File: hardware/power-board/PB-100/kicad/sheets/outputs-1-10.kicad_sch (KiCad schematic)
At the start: 40 parts, among them J101 OUTPUT_CONNECTOR_CLASS_PRELIM, J102 OUTPUT_CONNECTOR_CLASS_PRELIM, J103 OUTPUT_CONNECTOR_CLASS_PRELIM, J104 OUTPUT_CONNECTOR_CLASS_PRELIM, J105 OUTPUT_CONNECTOR_CLASS_PRELIM, J106 OUTPUT_CONNECTOR_CLASS_PRELIM, J107 OUTPUT_CONNECTOR_CLASS_PRELIM, J108 OUTPUT_CONNECTOR_CLASS_PRELIM, J109 OUTPUT_CONNECTOR_CLASS_PRELIM, J110 OUTPUT_CONNECTOR_CLASS_PRELIM, Q101 SIDR626LDP_PRELIM, Q102 SIDR626LDP_PRELIM, Q103 SIDR626LDP_PRELIM, Q104 SIDR626LDP_PRELIM, Q105 SIDR626LDP_PRELIM, Q106 SIDR626LDP_PRELIM, Q107 SIDR626LDP_PRELIM, Q108 SIDR626LDP_PRELIM, Q109 SIDR626LDP_PRELIM, Q110 SIDR626LDP_PRELIM, U101 TPS48110AQDGXRQ1_PRELIM, U102 TPS48110AQDGXRQ1_PRELIM, U103 TPS48110AQDGXRQ1_PRELIM, U104 TPS48110AQDGXRQ1_PRELIM, U105 TPS48110AQDGXRQ1_PRELIM, U106 TPS48110AQDGXRQ1_PRELIM, U107 TPS48110AQDGXRQ1_PRELIM, U108 TPS48110AQDGXRQ1_PRELIM, U109 TPS48110AQDGXRQ1_PRELIM, U110 TPS48110AQDGXRQ1_PRELIM

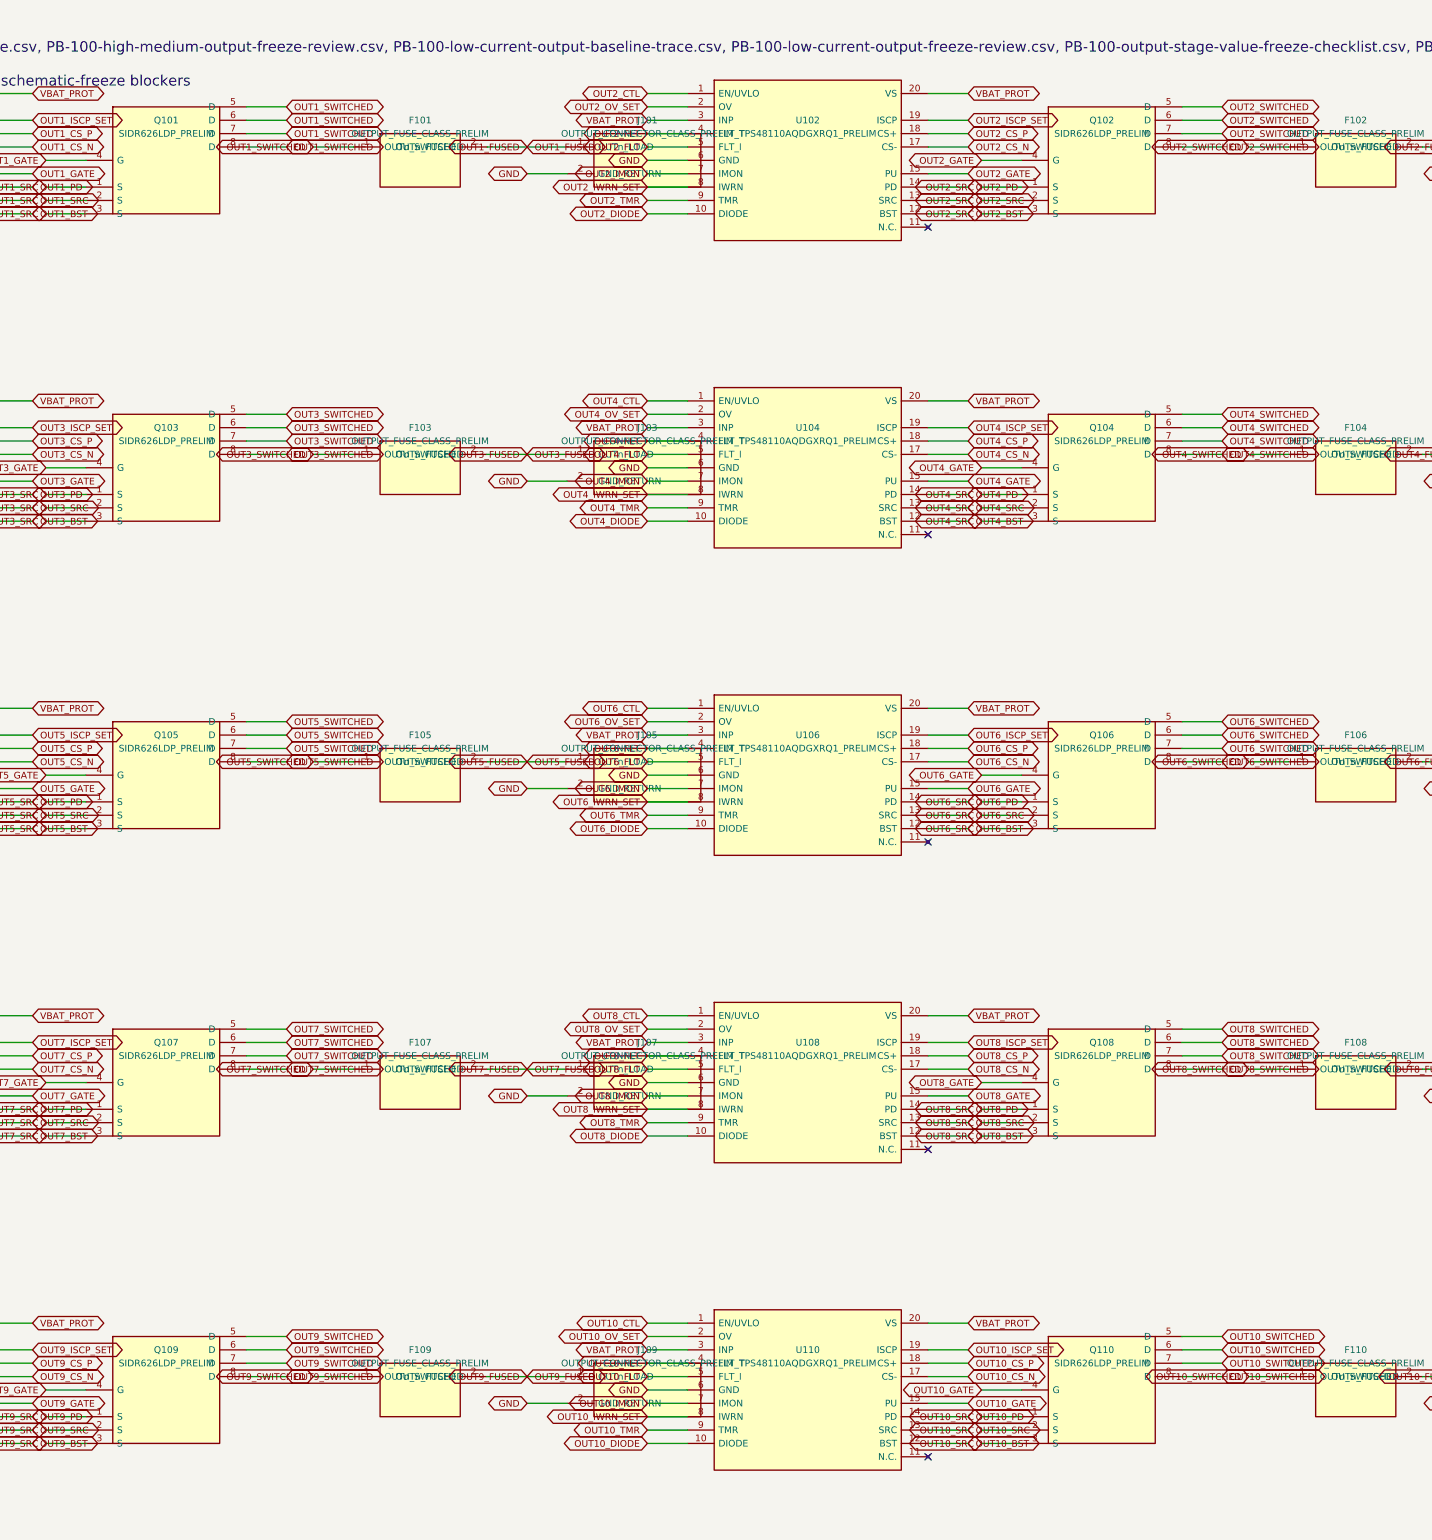
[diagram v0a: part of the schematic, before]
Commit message: feat(hardware): accept CAN1 and 80V freeze decisions
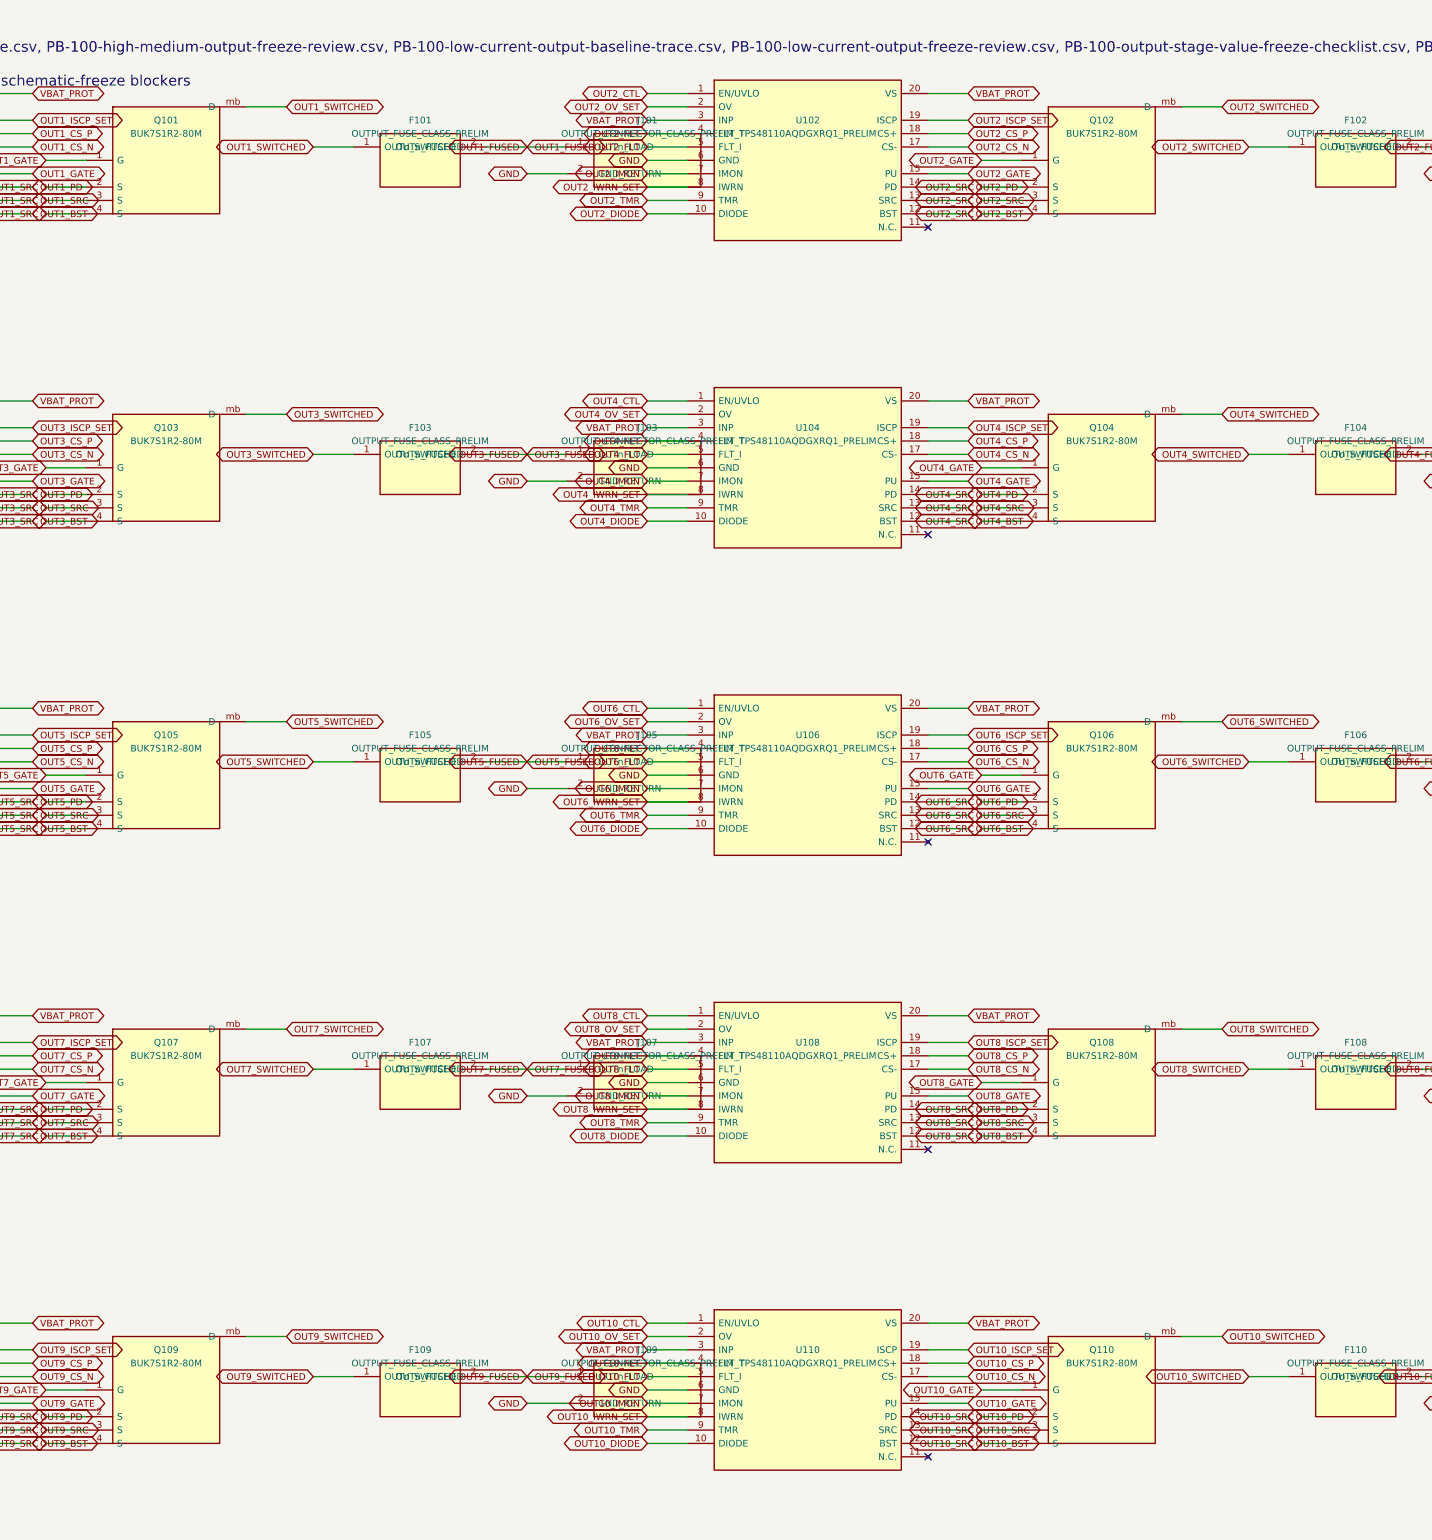
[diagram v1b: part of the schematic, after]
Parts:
- Q101, Q102, Q103, Q104, Q105, Q106, Q107, Q108, Q109, Q110: value SIDR626LDP_PRELIM -> BUK7S1R2-80M; footprint (none) -> PB100:LFPAK88_SOT1235_Nexperia; symbol PB100:PB100_SIDR626LDP_PRELIM -> PB100:PB100_POWER_NMOS_ESCAPE_PRELIM
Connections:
- net OUT10_GATE: now also Q110.1 (G); no longer Q110.4 (G)
- net OUT10_SRC: now also Q110.4 (S); no longer Q110.1 (S)
- net OUT10_SWITCHED: now also Q110.mb (D); no longer Q110.5 (D), Q110.6 (D), Q110.7 (D), Q110.8 (D)
- net OUT1_GATE: now also Q101.1 (G); no longer Q101.4 (G)
- net OUT1_SRC: now also Q101.4 (S); no longer Q101.1 (S)
- net OUT1_SWITCHED: now also Q101.mb (D); no longer Q101.5 (D), Q101.6 (D), Q101.7 (D), Q101.8 (D)
- net OUT2_GATE: now also Q102.1 (G); no longer Q102.4 (G)
- net OUT2_SRC: now also Q102.4 (S); no longer Q102.1 (S)
- net OUT2_SWITCHED: now also Q102.mb (D); no longer Q102.5 (D), Q102.6 (D), Q102.7 (D), Q102.8 (D)
- net OUT3_GATE: now also Q103.1 (G); no longer Q103.4 (G)
- net OUT3_SRC: now also Q103.4 (S); no longer Q103.1 (S)
- net OUT3_SWITCHED: now also Q103.mb (D); no longer Q103.5 (D), Q103.6 (D), Q103.7 (D), Q103.8 (D)
- net OUT4_GATE: now also Q104.1 (G); no longer Q104.4 (G)
- net OUT4_SRC: now also Q104.4 (S); no longer Q104.1 (S)
- net OUT4_SWITCHED: now also Q104.mb (D); no longer Q104.5 (D), Q104.6 (D), Q104.7 (D), Q104.8 (D)
- net OUT5_GATE: now also Q105.1 (G); no longer Q105.4 (G)
- net OUT5_SRC: now also Q105.4 (S); no longer Q105.1 (S)
- net OUT5_SWITCHED: now also Q105.mb (D); no longer Q105.5 (D), Q105.6 (D), Q105.7 (D), Q105.8 (D)
- net OUT6_GATE: now also Q106.1 (G); no longer Q106.4 (G)
- net OUT6_SRC: now also Q106.4 (S); no longer Q106.1 (S)
- net OUT6_SWITCHED: now also Q106.mb (D); no longer Q106.5 (D), Q106.6 (D), Q106.7 (D), Q106.8 (D)
- net OUT7_GATE: now also Q107.1 (G); no longer Q107.4 (G)
- net OUT7_SRC: now also Q107.4 (S); no longer Q107.1 (S)
- net OUT7_SWITCHED: now also Q107.mb (D); no longer Q107.5 (D), Q107.6 (D), Q107.7 (D), Q107.8 (D)
- net OUT8_GATE: now also Q108.1 (G); no longer Q108.4 (G)
- net OUT8_SRC: now also Q108.4 (S); no longer Q108.1 (S)
- net OUT8_SWITCHED: now also Q108.mb (D); no longer Q108.5 (D), Q108.6 (D), Q108.7 (D), Q108.8 (D)
- net OUT9_GATE: now also Q109.1 (G); no longer Q109.4 (G)
- net OUT9_SRC: now also Q109.4 (S); no longer Q109.1 (S)
- net OUT9_SWITCHED: now also Q109.mb (D); no longer Q109.5 (D), Q109.6 (D), Q109.7 (D), Q109.8 (D)

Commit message: feat(pb100): close five pre-layout blockers with generated evidence
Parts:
- Q101, Q102, Q103, Q104, Q105, Q106, Q107, Q108, Q109, Q110: value BUK7S1R2-80M -> IAUT300N08S5N012ATMA2; footprint PB100:LFPAK88_SOT1235_Nexperia -> PB100:PG-HSOF-8-1_TOLL_Infineon; symbol PB100:PB100_POWER_NMOS_ESCAPE_PRELIM -> PB100:PB100_POWER_NMOS_TOLL_80V
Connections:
- net OUT10_SRC: now also Q110.5 (S), Q110.6 (S), Q110.7 (S), Q110.8 (S)
- net OUT10_SWITCHED: now also Q110.Tab (D); no longer Q110.mb (D)
- net OUT1_SRC: now also Q101.5 (S), Q101.6 (S), Q101.7 (S), Q101.8 (S)
- net OUT1_SWITCHED: now also Q101.Tab (D); no longer Q101.mb (D)
- net OUT2_SRC: now also Q102.5 (S), Q102.6 (S), Q102.7 (S), Q102.8 (S)
- net OUT2_SWITCHED: now also Q102.Tab (D); no longer Q102.mb (D)
- net OUT3_SRC: now also Q103.5 (S), Q103.6 (S), Q103.7 (S), Q103.8 (S)
- net OUT3_SWITCHED: now also Q103.Tab (D); no longer Q103.mb (D)
- net OUT4_SRC: now also Q104.5 (S), Q104.6 (S), Q104.7 (S), Q104.8 (S)
- net OUT4_SWITCHED: now also Q104.Tab (D); no longer Q104.mb (D)
- net OUT5_SRC: now also Q105.5 (S), Q105.6 (S), Q105.7 (S), Q105.8 (S)
- net OUT5_SWITCHED: now also Q105.Tab (D); no longer Q105.mb (D)
- net OUT6_SRC: now also Q106.5 (S), Q106.6 (S), Q106.7 (S), Q106.8 (S)
- net OUT6_SWITCHED: now also Q106.Tab (D); no longer Q106.mb (D)
- net OUT7_SRC: now also Q107.5 (S), Q107.6 (S), Q107.7 (S), Q107.8 (S)
- net OUT7_SWITCHED: now also Q107.Tab (D); no longer Q107.mb (D)
- net OUT8_SRC: now also Q108.5 (S), Q108.6 (S), Q108.7 (S), Q108.8 (S)
- net OUT8_SWITCHED: now also Q108.Tab (D); no longer Q108.mb (D)
- net OUT9_SRC: now also Q109.5 (S), Q109.6 (S), Q109.7 (S), Q109.8 (S)
- net OUT9_SWITCHED: now also Q109.Tab (D); no longer Q109.mb (D)

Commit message: Advance PB-100 EVT routing baseline
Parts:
- removed F101, F102, F103, F104, F105, F106, F107, F108, F109, F110: OUTPUT_FUSE_CLASS_PRELIM, symbol PB100:PB100_OUTPUT_FUSE_CLASS_PRELIM
- removed J101, J102, J103, J104, J105, J106, J107, J108, J109, J110: OUTPUT_CONNECTOR_CLASS_PRELIM, symbol PB100:PB100_OUTPUT_CONNECTOR_CLASS_PRELIM
- removed Q101, Q102, Q103, Q104, Q105, Q106, Q107, Q108, Q109, Q110: IAUT300N08S5N012ATMA2, PB100:PG-HSOF-8-1_TOLL_Infineon, symbol PB100:PB100_POWER_NMOS_TOLL_80V
- removed U101, U102, U103, U104, U105, U106, U107, U108, U109, U110: TPS48110AQDGXRQ1_PRELIM, symbol PB100:PB100_TPS48110AQDGXRQ1_PRELIM
- added C1101: 680nF 16V X7R TMR, PB100:C0603, symbol PB100Gen:PB100G_C1101
- added C1102: 470nF 25V X7R BST, PB100:C0603, symbol PB100Gen:PB100G_C1102
- added C1103: 1nF 50V C0G ISCP, PB100:C0603, symbol PB100Gen:PB100G_C1103
- added C1104: 100nF 100V X7R VS, PB100:C0805, symbol PB100Gen:PB100G_C1104
- added C1105: 10nF 50V X7R IMON, PB100:C0603, symbol PB100Gen:PB100G_C1105
- added C1106: 1nF 25V DNP GATE-SLEW, PB100:C0603, symbol PB100Gen:PB100G_C1106
- added C1107: 1nF 100V C0G DNP SNUBBER, PB100:C0603, symbol PB100Gen:PB100G_C1107
- added C1201: 680nF 16V X7R TMR, PB100:C0603, symbol PB100Gen:PB100G_C1201
- added C1202: 470nF 25V X7R BST, PB100:C0603, symbol PB100Gen:PB100G_C1202
- added C1203: 1nF 50V C0G ISCP, PB100:C0603, symbol PB100Gen:PB100G_C1203
- added C1204: 100nF 100V X7R VS, PB100:C0805, symbol PB100Gen:PB100G_C1204
- added C1205: 10nF 50V X7R IMON, PB100:C0603, symbol PB100Gen:PB100G_C1205
- added C1206: 1nF 25V DNP GATE-SLEW, PB100:C0603, symbol PB100Gen:PB100G_C1206
- added C1207: 1nF 100V C0G DNP SNUBBER, PB100:C0603, symbol PB100Gen:PB100G_C1207
- added C1301: 680nF 16V X7R TMR, PB100:C0603, symbol PB100Gen:PB100G_C1301
- added C1302: 470nF 25V X7R BST, PB100:C0603, symbol PB100Gen:PB100G_C1302
- added C1303: 1nF 50V C0G ISCP, PB100:C0603, symbol PB100Gen:PB100G_C1303
- added C1304: 100nF 100V X7R VS, PB100:C0805, symbol PB100Gen:PB100G_C1304
- added C1305: 10nF 50V X7R IMON, PB100:C0603, symbol PB100Gen:PB100G_C1305
- added C1306: 1nF 25V DNP GATE-SLEW, PB100:C0603, symbol PB100Gen:PB100G_C1306
- added C1307: 1nF 100V C0G DNP SNUBBER, PB100:C0603, symbol PB100Gen:PB100G_C1307
- added C1401: 680nF 16V X7R TMR, PB100:C0603, symbol PB100Gen:PB100G_C1401
- added C1402: 470nF 25V X7R BST, PB100:C0603, symbol PB100Gen:PB100G_C1402
- added C1403: 1nF 50V C0G ISCP, PB100:C0603, symbol PB100Gen:PB100G_C1403
- added C1404: 100nF 100V X7R VS, PB100:C0805, symbol PB100Gen:PB100G_C1404
- added C1405: 10nF 50V X7R IMON, PB100:C0603, symbol PB100Gen:PB100G_C1405
- added C1406: 1nF 25V DNP GATE-SLEW, PB100:C0603, symbol PB100Gen:PB100G_C1406
- added C1407: 1nF 100V C0G DNP SNUBBER, PB100:C0603, symbol PB100Gen:PB100G_C1407
- added C1501: 680nF 16V X7R TMR, PB100:C0603, symbol PB100Gen:PB100G_C1501
- added C1502: 470nF 25V X7R BST, PB100:C0603, symbol PB100Gen:PB100G_C1502
- added C1503: 1nF 50V C0G ISCP, PB100:C0603, symbol PB100Gen:PB100G_C1503
- added C1504: 100nF 100V X7R VS, PB100:C0805, symbol PB100Gen:PB100G_C1504
- added C1505: 10nF 50V X7R IMON, PB100:C0603, symbol PB100Gen:PB100G_C1505
- added C1506: 1nF 25V DNP GATE-SLEW, PB100:C0603, symbol PB100Gen:PB100G_C1506
- added C1507: 1nF 100V C0G DNP SNUBBER, PB100:C0603, symbol PB100Gen:PB100G_C1507
- added C1601: 680nF 16V X7R TMR, PB100:C0603, symbol PB100Gen:PB100G_C1601
- added C1602: 470nF 25V X7R BST, PB100:C0603, symbol PB100Gen:PB100G_C1602
- added C1603: 1nF 50V C0G ISCP, PB100:C0603, symbol PB100Gen:PB100G_C1603
- added C1604: 100nF 100V X7R VS, PB100:C0805, symbol PB100Gen:PB100G_C1604
- added C1605: 10nF 50V X7R IMON, PB100:C0603, symbol PB100Gen:PB100G_C1605
- added C1606: 1nF 25V DNP GATE-SLEW, PB100:C0603, symbol PB100Gen:PB100G_C1606
- added C1607: 1nF 100V C0G DNP SNUBBER, PB100:C0603, symbol PB100Gen:PB100G_C1607
- added C1701: 680nF 16V X7R TMR, PB100:C0603, symbol PB100Gen:PB100G_C1701
- added C1702: 470nF 25V X7R BST, PB100:C0603, symbol PB100Gen:PB100G_C1702
- added C1703: 1nF 50V C0G ISCP, PB100:C0603, symbol PB100Gen:PB100G_C1703
- added C1704: 100nF 100V X7R VS, PB100:C0805, symbol PB100Gen:PB100G_C1704
- added C1705: 10nF 50V X7R IMON, PB100:C0603, symbol PB100Gen:PB100G_C1705
- added C1706: 1nF 25V DNP GATE-SLEW, PB100:C0603, symbol PB100Gen:PB100G_C1706
- added C1707: 1nF 100V C0G DNP SNUBBER, PB100:C0603, symbol PB100Gen:PB100G_C1707
- added C1801: 680nF 16V X7R TMR, PB100:C0603, symbol PB100Gen:PB100G_C1801
- added C1802: 470nF 25V X7R BST, PB100:C0603, symbol PB100Gen:PB100G_C1802
- added C1803: 1nF 50V C0G ISCP, PB100:C0603, symbol PB100Gen:PB100G_C1803
- added C1804: 100nF 100V X7R VS, PB100:C0805, symbol PB100Gen:PB100G_C1804
- added C1805: 10nF 50V X7R IMON, PB100:C0603, symbol PB100Gen:PB100G_C1805
- added C1806: 1nF 25V DNP GATE-SLEW, PB100:C0603, symbol PB100Gen:PB100G_C1806
- added C1807: 1nF 100V C0G DNP SNUBBER, PB100:C0603, symbol PB100Gen:PB100G_C1807
- added C1901: 680nF 16V X7R TMR, PB100:C0603, symbol PB100Gen:PB100G_C1901
- added C1902: 470nF 25V X7R BST, PB100:C0603, symbol PB100Gen:PB100G_C1902
- added C1903: 1nF 50V C0G ISCP, PB100:C0603, symbol PB100Gen:PB100G_C1903
- added C1904: 100nF 100V X7R VS, PB100:C0805, symbol PB100Gen:PB100G_C1904
- added C1905: 10nF 50V X7R IMON, PB100:C0603, symbol PB100Gen:PB100G_C1905
- added C1906: 1nF 25V DNP GATE-SLEW, PB100:C0603, symbol PB100Gen:PB100G_C1906
- added C1907: 1nF 100V C0G DNP SNUBBER, PB100:C0603, symbol PB100Gen:PB100G_C1907
- added C2001: 680nF 16V X7R TMR, PB100:C0603, symbol PB100Gen:PB100G_C2001
- added C2002: 470nF 25V X7R BST, PB100:C0603, symbol PB100Gen:PB100G_C2002
- added C2003: 1nF 50V C0G ISCP, PB100:C0603, symbol PB100Gen:PB100G_C2003
- added C2004: 100nF 100V X7R VS, PB100:C0805, symbol PB100Gen:PB100G_C2004
- added C2005: 10nF 50V X7R IMON, PB100:C0603, symbol PB100Gen:PB100G_C2005
- added C2006: 1nF 25V DNP GATE-SLEW, PB100:C0603, symbol PB100Gen:PB100G_C2006
- added C2007: 1nF 100V C0G DNP SNUBBER, PB100:C0603, symbol PB100Gen:PB100G_C2007
- added DCL101: STPS40170CGY-TR 2x20A 170V COMMON-CATHODE, PB100:D2PAK_3_CommonCathode, symbol PB100Gen:PB100G_DCL101
- added DCL102: STPS40170CGY-TR 2x20A 170V COMMON-CATHODE, PB100:D2PAK_3_CommonCathode, symbol PB100Gen:PB100G_DCL102
- added DCL103: STPS40170CGY-TR 2x20A 170V COMMON-CATHODE, PB100:D2PAK_3_CommonCathode, symbol PB100Gen:PB100G_DCL103
- added DCL104: STPS40170CGY-TR 2x20A 170V COMMON-CATHODE, PB100:D2PAK_3_CommonCathode, symbol PB100Gen:PB100G_DCL104
- added DCL105: STPS40170CGY-TR 2x20A 170V COMMON-CATHODE, PB100:D2PAK_3_CommonCathode, symbol PB100Gen:PB100G_DCL105
- added DCL106: STPS40170CGY-TR 2x20A 170V COMMON-CATHODE, PB100:D2PAK_3_CommonCathode, symbol PB100Gen:PB100G_DCL106
- added DCL107: STPS40170CGY-TR 2x20A 170V COMMON-CATHODE, PB100:D2PAK_3_CommonCathode, symbol PB100Gen:PB100G_DCL107
- added DCL108: STPS40170CGY-TR 2x20A 170V COMMON-CATHODE, PB100:D2PAK_3_CommonCathode, symbol PB100Gen:PB100G_DCL108
- added DCL109: STPS40170CGY-TR 2x20A 170V COMMON-CATHODE, PB100:D2PAK_3_CommonCathode, symbol PB100Gen:PB100G_DCL109
- added DCL110: STPS40170CGY-TR 2x20A 170V COMMON-CATHODE, PB100:D2PAK_3_CommonCathode, symbol PB100Gen:PB100G_DCL110
- added F101: OUTPUT_FUSE_CLASS_PRELIM (OFF-BOARD), symbol PB100Gen:PB100G_F101
- added F102: OUTPUT_FUSE_CLASS_PRELIM (OFF-BOARD), symbol PB100Gen:PB100G_F102
- added F103: OUTPUT_FUSE_CLASS_PRELIM (OFF-BOARD), symbol PB100Gen:PB100G_F103
- added F104: OUTPUT_FUSE_CLASS_PRELIM (OFF-BOARD), symbol PB100Gen:PB100G_F104
- added F105: OUTPUT_FUSE_CLASS_PRELIM (OFF-BOARD), symbol PB100Gen:PB100G_F105
- added F106: OUTPUT_FUSE_CLASS_PRELIM (OFF-BOARD), symbol PB100Gen:PB100G_F106
- added F107: OUTPUT_FUSE_CLASS_PRELIM (OFF-BOARD), symbol PB100Gen:PB100G_F107
- added F108: OUTPUT_FUSE_CLASS_PRELIM (OFF-BOARD), symbol PB100Gen:PB100G_F108
- added F109: OUTPUT_FUSE_CLASS_PRELIM (OFF-BOARD), symbol PB100Gen:PB100G_F109
- added F110: OUTPUT_FUSE_CLASS_PRELIM (OFF-BOARD), symbol PB100Gen:PB100G_F110
- added J101: OUTPUT_CONNECTOR_CLASS_PRELIM (OFF-BOARD), symbol PB100Gen:PB100G_J101
- added J102: OUTPUT_CONNECTOR_CLASS_PRELIM (OFF-BOARD), symbol PB100Gen:PB100G_J102
- added J103: OUTPUT_CONNECTOR_CLASS_PRELIM (OFF-BOARD), symbol PB100Gen:PB100G_J103
- added J104: OUTPUT_CONNECTOR_CLASS_PRELIM (OFF-BOARD), symbol PB100Gen:PB100G_J104
- added J105: OUTPUT_CONNECTOR_CLASS_PRELIM (OFF-BOARD), symbol PB100Gen:PB100G_J105
- added J106: OUTPUT_CONNECTOR_CLASS_PRELIM (OFF-BOARD), symbol PB100Gen:PB100G_J106
- added J107: OUTPUT_CONNECTOR_CLASS_PRELIM (OFF-BOARD), symbol PB100Gen:PB100G_J107
- added J108: OUTPUT_CONNECTOR_CLASS_PRELIM (OFF-BOARD), symbol PB100Gen:PB100G_J108
- added J109: OUTPUT_CONNECTOR_CLASS_PRELIM (OFF-BOARD), symbol PB100Gen:PB100G_J109
- added J110: OUTPUT_CONNECTOR_CLASS_PRELIM (OFF-BOARD), symbol PB100Gen:PB100G_J110
- added Q101: IAUT300N08S5N012ATMA2, PB100:PG-HSOF-8-1_TOLL_Infineon, symbol PB100Gen:PB100G_Q101
- added Q102: IAUT300N08S5N012ATMA2, PB100:PG-HSOF-8-1_TOLL_Infineon, symbol PB100Gen:PB100G_Q102
- added Q103: IAUT300N08S5N012ATMA2, PB100:PG-HSOF-8-1_TOLL_Infineon, symbol PB100Gen:PB100G_Q103
- added Q104: IAUT300N08S5N012ATMA2, PB100:PG-HSOF-8-1_TOLL_Infineon, symbol PB100Gen:PB100G_Q104
- added Q105: IAUT300N08S5N012ATMA2, PB100:PG-HSOF-8-1_TOLL_Infineon, symbol PB100Gen:PB100G_Q105
- added Q106: IAUT300N08S5N012ATMA2, PB100:PG-HSOF-8-1_TOLL_Infineon, symbol PB100Gen:PB100G_Q106
- added Q107: IAUT300N08S5N012ATMA2, PB100:PG-HSOF-8-1_TOLL_Infineon, symbol PB100Gen:PB100G_Q107
- added Q108: IAUT300N08S5N012ATMA2, PB100:PG-HSOF-8-1_TOLL_Infineon, symbol PB100Gen:PB100G_Q108
- added Q109: IAUT300N08S5N012ATMA2, PB100:PG-HSOF-8-1_TOLL_Infineon, symbol PB100Gen:PB100G_Q109
- added Q110: IAUT300N08S5N012ATMA2, PB100:PG-HSOF-8-1_TOLL_Infineon, symbol PB100Gen:PB100G_Q110
- added QT101: MMBT3904-Q REMOTE TEMP DIODE, PB100:SOT-23-3_DBZ_TI, symbol PB100Gen:PB100G_QT101
- added QT102: MMBT3904-Q REMOTE TEMP DIODE, PB100:SOT-23-3_DBZ_TI, symbol PB100Gen:PB100G_QT102
- added QT103: MMBT3904-Q REMOTE TEMP DIODE, PB100:SOT-23-3_DBZ_TI, symbol PB100Gen:PB100G_QT103
- added QT104: MMBT3904-Q REMOTE TEMP DIODE, PB100:SOT-23-3_DBZ_TI, symbol PB100Gen:PB100G_QT104
- added QT105: MMBT3904-Q REMOTE TEMP DIODE, PB100:SOT-23-3_DBZ_TI, symbol PB100Gen:PB100G_QT105
- added QT106: MMBT3904-Q REMOTE TEMP DIODE, PB100:SOT-23-3_DBZ_TI, symbol PB100Gen:PB100G_QT106
- added QT107: MMBT3904-Q REMOTE TEMP DIODE, PB100:SOT-23-3_DBZ_TI, symbol PB100Gen:PB100G_QT107
- added QT108: MMBT3904-Q REMOTE TEMP DIODE, PB100:SOT-23-3_DBZ_TI, symbol PB100Gen:PB100G_QT108
- added QT109: MMBT3904-Q REMOTE TEMP DIODE, PB100:SOT-23-3_DBZ_TI, symbol PB100Gen:PB100G_QT109
- added QT110: MMBT3904-Q REMOTE TEMP DIODE, PB100:SOT-23-3_DBZ_TI, symbol PB100Gen:PB100G_QT110
- added R1101: 470k 1%, PB100:R0603, symbol PB100Gen:PB100G_R1101
- added R1102: 103k 1%, PB100:R0603, symbol PB100Gen:PB100G_R1102
- added R1103: 12.4k 1%, PB100:R0603, symbol PB100Gen:PB100G_R1103
- added R1104: 100R 1% RSET, PB100:R0603, symbol PB100Gen:PB100G_R1104
- added R1105: 49.9k 1% RIWRN, PB100:R0603, symbol PB100Gen:PB100G_R1105
- added R1106: 3.40k 1% RISCP, PB100:R0603, symbol PB100Gen:PB100G_R1106
- added R1107: 12.1k 1% RIMON, PB100:R0603, symbol PB100Gen:PB100G_R1107
- added R1108: 1k 1% IMON ADC SERIES, PB100:R0603, symbol PB100Gen:PB100G_R1108
- added R1109: 100k CTL DEFAULT-OFF, PB100:R0603, symbol PB100Gen:PB100G_R1109
- added R1110: 3.3R 1% REPLACEABLE PU, PB100:R0603, symbol PB100Gen:PB100G_R1110
- added R1111: 0R REPLACEABLE PD, PB100:R0603, symbol PB100Gen:PB100G_R1111
- added R1112: 10k FLT PULL-UP, PB100:R0603, symbol PB100Gen:PB100G_R1112
- added R1113: 100R DNP DRAIN-SOURCE SNUBBER, PB100:R0603, symbol PB100Gen:PB100G_R1113
- added R1201: 470k 1%, PB100:R0603, symbol PB100Gen:PB100G_R1201
- added R1202: 103k 1%, PB100:R0603, symbol PB100Gen:PB100G_R1202
- added R1203: 12.4k 1%, PB100:R0603, symbol PB100Gen:PB100G_R1203
- added R1204: 100R 1% RSET, PB100:R0603, symbol PB100Gen:PB100G_R1204
- added R1205: 67.3k 1% RIWRN, PB100:R0603, symbol PB100Gen:PB100G_R1205
- added R1206: 2.61k 1% RISCP, PB100:R0603, symbol PB100Gen:PB100G_R1206
- added R1207: 12.1k 1% RIMON, PB100:R0603, symbol PB100Gen:PB100G_R1207
- added R1208: 1k 1% IMON ADC SERIES, PB100:R0603, symbol PB100Gen:PB100G_R1208
- added R1209: 100k CTL DEFAULT-OFF, PB100:R0603, symbol PB100Gen:PB100G_R1209
- added R1210: 3.3R 1% REPLACEABLE PU, PB100:R0603, symbol PB100Gen:PB100G_R1210
- added R1211: 0R REPLACEABLE PD, PB100:R0603, symbol PB100Gen:PB100G_R1211
- added R1212: 10k FLT PULL-UP, PB100:R0603, symbol PB100Gen:PB100G_R1212
- added R1213: 100R DNP DRAIN-SOURCE SNUBBER, PB100:R0603, symbol PB100Gen:PB100G_R1213
- added R1301: 470k 1%, PB100:R0603, symbol PB100Gen:PB100G_R1301
- added R1302: 103k 1%, PB100:R0603, symbol PB100Gen:PB100G_R1302
- added R1303: 12.4k 1%, PB100:R0603, symbol PB100Gen:PB100G_R1303
- added R1304: 100R 1% RSET, PB100:R0603, symbol PB100Gen:PB100G_R1304
- added R1305: 49.9k 1% RIWRN, PB100:R0603, symbol PB100Gen:PB100G_R1305
- added R1306: 3.83k 1% RISCP, PB100:R0603, symbol PB100Gen:PB100G_R1306
- added R1307: 12.1k 1% RIMON, PB100:R0603, symbol PB100Gen:PB100G_R1307
- added R1308: 1k 1% IMON ADC SERIES, PB100:R0603, symbol PB100Gen:PB100G_R1308
- added R1309: 100k CTL DEFAULT-OFF, PB100:R0603, symbol PB100Gen:PB100G_R1309
- added R1310: 3.3R 1% REPLACEABLE PU, PB100:R0603, symbol PB100Gen:PB100G_R1310
- added R1311: 0R REPLACEABLE PD, PB100:R0603, symbol PB100Gen:PB100G_R1311
- added R1312: 10k FLT PULL-UP, PB100:R0603, symbol PB100Gen:PB100G_R1312
- added R1313: 100R DNP DRAIN-SOURCE SNUBBER, PB100:R0603, symbol PB100Gen:PB100G_R1313
- added R1401: 470k 1%, PB100:R0603, symbol PB100Gen:PB100G_R1401
- added R1402: 103k 1%, PB100:R0603, symbol PB100Gen:PB100G_R1402
- added R1403: 12.4k 1%, PB100:R0603, symbol PB100Gen:PB100G_R1403
- added R1404: 100R 1% RSET, PB100:R0603, symbol PB100Gen:PB100G_R1404
- added R1405: 49.9k 1% RIWRN, PB100:R0603, symbol PB100Gen:PB100G_R1405
- added R1406: 3.83k 1% RISCP, PB100:R0603, symbol PB100Gen:PB100G_R1406
- added R1407: 12.1k 1% RIMON, PB100:R0603, symbol PB100Gen:PB100G_R1407
- added R1408: 1k 1% IMON ADC SERIES, PB100:R0603, symbol PB100Gen:PB100G_R1408
- added R1409: 100k CTL DEFAULT-OFF, PB100:R0603, symbol PB100Gen:PB100G_R1409
- added R1410: 3.3R 1% REPLACEABLE PU, PB100:R0603, symbol PB100Gen:PB100G_R1410
- added R1411: 0R REPLACEABLE PD, PB100:R0603, symbol PB100Gen:PB100G_R1411
- added R1412: 10k FLT PULL-UP, PB100:R0603, symbol PB100Gen:PB100G_R1412
- added R1413: 100R DNP DRAIN-SOURCE SNUBBER, PB100:R0603, symbol PB100Gen:PB100G_R1413
- added R1501: 470k 1%, PB100:R0603, symbol PB100Gen:PB100G_R1501
- added R1502: 103k 1%, PB100:R0603, symbol PB100Gen:PB100G_R1502
- added R1503: 12.4k 1%, PB100:R0603, symbol PB100Gen:PB100G_R1503
- added R1504: 100R 1% RSET, PB100:R0603, symbol PB100Gen:PB100G_R1504
- added R1505: 49.9k 1% RIWRN, PB100:R0603, symbol PB100Gen:PB100G_R1505
- added R1506: 3.74k 1% RISCP, PB100:R0603, symbol PB100Gen:PB100G_R1506
- added R1507: 12.1k 1% RIMON, PB100:R0603, symbol PB100Gen:PB100G_R1507
- added R1508: 1k 1% IMON ADC SERIES, PB100:R0603, symbol PB100Gen:PB100G_R1508
- added R1509: 100k CTL DEFAULT-OFF, PB100:R0603, symbol PB100Gen:PB100G_R1509
- added R1510: 3.3R 1% REPLACEABLE PU, PB100:R0603, symbol PB100Gen:PB100G_R1510
- added R1511: 0R REPLACEABLE PD, PB100:R0603, symbol PB100Gen:PB100G_R1511
- added R1512: 10k FLT PULL-UP, PB100:R0603, symbol PB100Gen:PB100G_R1512
- added R1513: 100R DNP DRAIN-SOURCE SNUBBER, PB100:R0603, symbol PB100Gen:PB100G_R1513
- added R1601: 470k 1%, PB100:R0603, symbol PB100Gen:PB100G_R1601
- added R1602: 103k 1%, PB100:R0603, symbol PB100Gen:PB100G_R1602
- added R1603: 12.4k 1%, PB100:R0603, symbol PB100Gen:PB100G_R1603
- added R1604: 100R 1% RSET, PB100:R0603, symbol PB100Gen:PB100G_R1604
- added R1605: 49.9k 1% RIWRN, PB100:R0603, symbol PB100Gen:PB100G_R1605
- added R1606: 3.83k 1% RISCP, PB100:R0603, symbol PB100Gen:PB100G_R1606
- added R1607: 12.1k 1% RIMON, PB100:R0603, symbol PB100Gen:PB100G_R1607
- added R1608: 1k 1% IMON ADC SERIES, PB100:R0603, symbol PB100Gen:PB100G_R1608
- added R1609: 100k CTL DEFAULT-OFF, PB100:R0603, symbol PB100Gen:PB100G_R1609
- added R1610: 3.3R 1% REPLACEABLE PU, PB100:R0603, symbol PB100Gen:PB100G_R1610
- added R1611: 0R REPLACEABLE PD, PB100:R0603, symbol PB100Gen:PB100G_R1611
- added R1612: 10k FLT PULL-UP, PB100:R0603, symbol PB100Gen:PB100G_R1612
- added R1613: 100R DNP DRAIN-SOURCE SNUBBER, PB100:R0603, symbol PB100Gen:PB100G_R1613
- added R1701: 470k 1%, PB100:R0603, symbol PB100Gen:PB100G_R1701
- added R1702: 103k 1%, PB100:R0603, symbol PB100Gen:PB100G_R1702
- added R1703: 12.4k 1%, PB100:R0603, symbol PB100Gen:PB100G_R1703
- added R1704: 100R 1% RSET, PB100:R0603, symbol PB100Gen:PB100G_R1704
- added R1705: 49.9k 1% RIWRN, PB100:R0603, symbol PB100Gen:PB100G_R1705
- added R1706: 3.83k 1% RISCP, PB100:R0603, symbol PB100Gen:PB100G_R1706
- added R1707: 12.1k 1% RIMON, PB100:R0603, symbol PB100Gen:PB100G_R1707
- added R1708: 1k 1% IMON ADC SERIES, PB100:R0603, symbol PB100Gen:PB100G_R1708
- added R1709: 100k CTL DEFAULT-OFF, PB100:R0603, symbol PB100Gen:PB100G_R1709
- added R1710: 3.3R 1% REPLACEABLE PU, PB100:R0603, symbol PB100Gen:PB100G_R1710
- added R1711: 0R REPLACEABLE PD, PB100:R0603, symbol PB100Gen:PB100G_R1711
- added R1712: 10k FLT PULL-UP, PB100:R0603, symbol PB100Gen:PB100G_R1712
- added R1713: 100R DNP DRAIN-SOURCE SNUBBER, PB100:R0603, symbol PB100Gen:PB100G_R1713
- added R1801: 470k 1%, PB100:R0603, symbol PB100Gen:PB100G_R1801
- added R1802: 103k 1%, PB100:R0603, symbol PB100Gen:PB100G_R1802
- added R1803: 12.4k 1%, PB100:R0603, symbol PB100Gen:PB100G_R1803
- added R1804: 100R 1% RSET, PB100:R0603, symbol PB100Gen:PB100G_R1804
- added R1805: 49.9k 1% RIWRN, PB100:R0603, symbol PB100Gen:PB100G_R1805
- added R1806: 3.74k 1% RISCP, PB100:R0603, symbol PB100Gen:PB100G_R1806
- added R1807: 12.1k 1% RIMON, PB100:R0603, symbol PB100Gen:PB100G_R1807
- added R1808: 1k 1% IMON ADC SERIES, PB100:R0603, symbol PB100Gen:PB100G_R1808
- added R1809: 100k CTL DEFAULT-OFF, PB100:R0603, symbol PB100Gen:PB100G_R1809
- added R1810: 3.3R 1% REPLACEABLE PU, PB100:R0603, symbol PB100Gen:PB100G_R1810
- added R1811: 0R REPLACEABLE PD, PB100:R0603, symbol PB100Gen:PB100G_R1811
- added R1812: 10k FLT PULL-UP, PB100:R0603, symbol PB100Gen:PB100G_R1812
- added R1813: 100R DNP DRAIN-SOURCE SNUBBER, PB100:R0603, symbol PB100Gen:PB100G_R1813
- added R1901: 470k 1%, PB100:R0603, symbol PB100Gen:PB100G_R1901
- added R1902: 103k 1%, PB100:R0603, symbol PB100Gen:PB100G_R1902
- added R1903: 12.4k 1%, PB100:R0603, symbol PB100Gen:PB100G_R1903
- added R1904: 100R 1% RSET, PB100:R0603, symbol PB100Gen:PB100G_R1904
- added R1905: 49.9k 1% RIWRN, PB100:R0603, symbol PB100Gen:PB100G_R1905
- added R1906: 3.74k 1% RISCP, PB100:R0603, symbol PB100Gen:PB100G_R1906
- added R1907: 12.1k 1% RIMON, PB100:R0603, symbol PB100Gen:PB100G_R1907
- added R1908: 1k 1% IMON ADC SERIES, PB100:R0603, symbol PB100Gen:PB100G_R1908
- added R1909: 100k CTL DEFAULT-OFF, PB100:R0603, symbol PB100Gen:PB100G_R1909
- added R1910: 3.3R 1% REPLACEABLE PU, PB100:R0603, symbol PB100Gen:PB100G_R1910
- added R1911: 0R REPLACEABLE PD, PB100:R0603, symbol PB100Gen:PB100G_R1911
- added R1912: 10k FLT PULL-UP, PB100:R0603, symbol PB100Gen:PB100G_R1912
- added R1913: 100R DNP DRAIN-SOURCE SNUBBER, PB100:R0603, symbol PB100Gen:PB100G_R1913
- added R2001: 470k 1%, PB100:R0603, symbol PB100Gen:PB100G_R2001
- added R2002: 103k 1%, PB100:R0603, symbol PB100Gen:PB100G_R2002
- added R2003: 12.4k 1%, PB100:R0603, symbol PB100Gen:PB100G_R2003
- added R2004: 100R 1% RSET, PB100:R0603, symbol PB100Gen:PB100G_R2004
- added R2005: 49.9k 1% RIWRN, PB100:R0603, symbol PB100Gen:PB100G_R2005
- added R2006: 3.83k 1% RISCP, PB100:R0603, symbol PB100Gen:PB100G_R2006
- added R2007: 12.1k 1% RIMON, PB100:R0603, symbol PB100Gen:PB100G_R2007
- added R2008: 1k 1% IMON ADC SERIES, PB100:R0603, symbol PB100Gen:PB100G_R2008
- added R2009: 100k CTL DEFAULT-OFF, PB100:R0603, symbol PB100Gen:PB100G_R2009
- added R2010: 3.3R 1% REPLACEABLE PU, PB100:R0603, symbol PB100Gen:PB100G_R2010
- added R2011: 0R REPLACEABLE PD, PB100:R0603, symbol PB100Gen:PB100G_R2011
- added R2012: 10k FLT PULL-UP, PB100:R0603, symbol PB100Gen:PB100G_R2012
- added R2013: 100R DNP DRAIN-SOURCE SNUBBER, PB100:R0603, symbol PB100Gen:PB100G_R2013
- added RSH101: CSS4J-4026 1.0mR FOUR-TERMINAL, PB100:CSS4J-4026_Bourns, symbol PB100Gen:PB100G_RSH101
- added RSH102: CSS4J-4026 0.5mR FOUR-TERMINAL, PB100:CSS4J-4026_Bourns, symbol PB100Gen:PB100G_RSH102
- added RSH103: CSS4J-4026 1.5mR FOUR-TERMINAL, PB100:CSS4J-4026_Bourns, symbol PB100Gen:PB100G_RSH103
- added RSH104: CSS4J-4026 1.5mR FOUR-TERMINAL, PB100:CSS4J-4026_Bourns, symbol PB100Gen:PB100G_RSH104
- added RSH105: CSS4J-4026 3.0mR FOUR-TERMINAL, PB100:CSS4J-4026_Bourns, symbol PB100Gen:PB100G_RSH105
- added RSH106: CSS4J-4026 1.5mR FOUR-TERMINAL, PB100:CSS4J-4026_Bourns, symbol PB100Gen:PB100G_RSH106
- added RSH107: CSS4J-4026 1.5mR FOUR-TERMINAL, PB100:CSS4J-4026_Bourns, symbol PB100Gen:PB100G_RSH107
- added RSH108: CSS4J-4026 3.0mR FOUR-TERMINAL, PB100:CSS4J-4026_Bourns, symbol PB100Gen:PB100G_RSH108
- added RSH109: CSS4J-4026 3.0mR FOUR-TERMINAL, PB100:CSS4J-4026_Bourns, symbol PB100Gen:PB100G_RSH109
- added RSH110: CSS4J-4026 1.5mR FOUR-TERMINAL, PB100:CSS4J-4026_Bourns, symbol PB100Gen:PB100G_RSH110
- added TP022: TEST OUT1_CTL, PB100:TestPoint_SMD_1.5mm, symbol PB100Gen:PB100G_TP022
- added TP023: TEST OUT1_FLT, PB100:TestPoint_SMD_1.5mm, symbol PB100Gen:PB100G_TP023
- added TP024: TEST OUT1_IMON, PB100:TestPoint_SMD_1.5mm, symbol PB100Gen:PB100G_TP024
- added TP025: TEST OUT1_SWITCHED, PB100:TestPoint_SMD_1.5mm, symbol PB100Gen:PB100G_TP025
- added TP026: TEST OUT2_CTL, PB100:TestPoint_SMD_1.5mm, symbol PB100Gen:PB100G_TP026
- added TP027: TEST OUT2_FLT, PB100:TestPoint_SMD_1.5mm, symbol PB100Gen:PB100G_TP027
- added TP028: TEST OUT2_IMON, PB100:TestPoint_SMD_1.5mm, symbol PB100Gen:PB100G_TP028
- added TP029: TEST OUT2_SWITCHED, PB100:TestPoint_SMD_1.5mm, symbol PB100Gen:PB100G_TP029
- added TP030: TEST OUT3_CTL, PB100:TestPoint_SMD_1.5mm, symbol PB100Gen:PB100G_TP030
- added TP031: TEST OUT3_FLT, PB100:TestPoint_SMD_1.5mm, symbol PB100Gen:PB100G_TP031
- added TP032: TEST OUT3_IMON, PB100:TestPoint_SMD_1.5mm, symbol PB100Gen:PB100G_TP032
- added TP033: TEST OUT3_SWITCHED, PB100:TestPoint_SMD_1.5mm, symbol PB100Gen:PB100G_TP033
- added TP034: TEST OUT4_CTL, PB100:TestPoint_SMD_1.5mm, symbol PB100Gen:PB100G_TP034
- added TP035: TEST OUT4_FLT, PB100:TestPoint_SMD_1.5mm, symbol PB100Gen:PB100G_TP035
- added TP036: TEST OUT4_IMON, PB100:TestPoint_SMD_1.5mm, symbol PB100Gen:PB100G_TP036
- added TP037: TEST OUT4_SWITCHED, PB100:TestPoint_SMD_1.5mm, symbol PB100Gen:PB100G_TP037
- added TP038: TEST OUT5_CTL, PB100:TestPoint_SMD_1.5mm, symbol PB100Gen:PB100G_TP038
- added TP039: TEST OUT5_FLT, PB100:TestPoint_SMD_1.5mm, symbol PB100Gen:PB100G_TP039
- added TP040: TEST OUT5_IMON, PB100:TestPoint_SMD_1.5mm, symbol PB100Gen:PB100G_TP040
- added TP041: TEST OUT5_SWITCHED, PB100:TestPoint_SMD_1.5mm, symbol PB100Gen:PB100G_TP041
- added TP042: TEST OUT6_CTL, PB100:TestPoint_SMD_1.5mm, symbol PB100Gen:PB100G_TP042
- added TP043: TEST OUT6_FLT, PB100:TestPoint_SMD_1.5mm, symbol PB100Gen:PB100G_TP043
- added TP044: TEST OUT6_IMON, PB100:TestPoint_SMD_1.5mm, symbol PB100Gen:PB100G_TP044
- added TP045: TEST OUT6_SWITCHED, PB100:TestPoint_SMD_1.5mm, symbol PB100Gen:PB100G_TP045
- added TP046: TEST OUT7_CTL, PB100:TestPoint_SMD_1.5mm, symbol PB100Gen:PB100G_TP046
- added TP047: TEST OUT7_FLT, PB100:TestPoint_SMD_1.5mm, symbol PB100Gen:PB100G_TP047
- added TP048: TEST OUT7_IMON, PB100:TestPoint_SMD_1.5mm, symbol PB100Gen:PB100G_TP048
- added TP049: TEST OUT7_SWITCHED, PB100:TestPoint_SMD_1.5mm, symbol PB100Gen:PB100G_TP049
- added TP050: TEST OUT8_CTL, PB100:TestPoint_SMD_1.5mm, symbol PB100Gen:PB100G_TP050
- added TP051: TEST OUT8_FLT, PB100:TestPoint_SMD_1.5mm, symbol PB100Gen:PB100G_TP051
- added TP052: TEST OUT8_IMON, PB100:TestPoint_SMD_1.5mm, symbol PB100Gen:PB100G_TP052
- added TP053: TEST OUT8_SWITCHED, PB100:TestPoint_SMD_1.5mm, symbol PB100Gen:PB100G_TP053
- added TP054: TEST OUT9_CTL, PB100:TestPoint_SMD_1.5mm, symbol PB100Gen:PB100G_TP054
- added TP055: TEST OUT9_FLT, PB100:TestPoint_SMD_1.5mm, symbol PB100Gen:PB100G_TP055
- added TP056: TEST OUT9_IMON, PB100:TestPoint_SMD_1.5mm, symbol PB100Gen:PB100G_TP056
- added TP057: TEST OUT9_SWITCHED, PB100:TestPoint_SMD_1.5mm, symbol PB100Gen:PB100G_TP057
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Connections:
- net GND: now also C1101.2, C1104.2, C1105.2, C1201.2, C1204.2, C1205.2, C1301.2, C1304.2, C1305.2, C1401.2, C1404.2, C1405.2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
- net OUT10_BST: now also C2002.1, U110.12 (BST)
- net OUT10_CS_N: now also C2003.2, RSH110.4 (SNS_OUT), U110.17 (CS-)
- net OUT10_CS_P: now also R2004.2, U110.18 (CS+)
- net OUT10_CTL: now also R2009.1, TP058.1 (OUT10_CTL), U110.3 (INP)
- net OUT10_DIODE: now also QT110.2 (B), QT110.3 (C), U110.10 (DIODE)
- net OUT10_FLT: now also R2012.2, TP059.1 (OUT10_FLT), U110.4 (FLT_T), U110.5 (FLT_I)
- net OUT10_FUSED: now also F110.2 (OUT), J110.1 (POS)
- net OUT10_GATE: now also C2006.1, Q110.1 (G), R2010.2, R2011.2
- net OUT10_IMON: now also C2005.1, R2008.2, TP060.1 (OUT10_IMON)
- net OUT10_PD: now also R2011.1, U110.14 (PD)
- net OUT10_SWITCHED: now also C2002.2, C2006.2, C2007.2, DCL110.2 (K), F110.1 (IN), Q110.2 (S), Q110.3 (S), Q110.4 (S), Q110.5 (S), Q110.6 (S), Q110.7 (S), Q110.8 (S)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
- net OUT10_TMR: now also C2001.1, U110.9 (TMR)
- net OUT1_BST: now also C1102.1, U101.12 (BST)
- net OUT1_CS_N: now also C1103.2, RSH101.4 (SNS_OUT), U101.17 (CS-)
- net OUT1_CS_P: now also R1104.2, U101.18 (CS+)
- net OUT1_CTL: now also R1109.1, TP022.1 (OUT1_CTL), U101.3 (INP)
- net OUT1_DIODE: now also QT101.2 (B), QT101.3 (C), U101.10 (DIODE)
- net OUT1_FLT: now also R1112.2, TP023.1 (OUT1_FLT), U101.4 (FLT_T), U101.5 (FLT_I)
- net OUT1_FUSED: now also F101.2 (OUT), J101.1 (POS)
- net OUT1_GATE: now also C1106.1, Q101.1 (G), R1110.2, R1111.2
- net OUT1_IMON: now also C1105.1, R1108.2, TP024.1 (OUT1_IMON)
- net OUT1_PD: now also R1111.1, U101.14 (PD)
- net OUT1_SWITCHED: now also C1102.2, C1106.2, C1107.2, DCL101.2 (K), F101.1 (IN), Q101.2 (S), Q101.3 (S), Q101.4 (S), Q101.5 (S), Q101.6 (S), Q101.7 (S), Q101.8 (S)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
- net OUT1_TMR: now also C1101.1, U101.9 (TMR)
- net OUT2_BST: now also C1202.1, U102.12 (BST)
- net OUT2_CS_N: now also C1203.2, RSH102.4 (SNS_OUT), U102.17 (CS-)
- net OUT2_CS_P: now also R1204.2, U102.18 (CS+)
- net OUT2_CTL: now also R1209.1, TP026.1 (OUT2_CTL), U102.3 (INP)
- net OUT2_DIODE: now also QT102.2 (B), QT102.3 (C), U102.10 (DIODE)
- net OUT2_FLT: now also R1212.2, TP027.1 (OUT2_FLT), U102.4 (FLT_T), U102.5 (FLT_I)
- net OUT2_FUSED: now also F102.2 (OUT), J102.1 (POS)
- net OUT2_GATE: now also C1206.1, Q102.1 (G), R1210.2, R1211.2
- net OUT2_IMON: now also C1205.1, R1208.2, TP028.1 (OUT2_IMON)
- net OUT2_PD: now also R1211.1, U102.14 (PD)
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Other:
- note added: "Work queue: CAP-OUT-INST. Ten role-free TPS48110-Q1 channels implement the accepted 80 V TOLL architecture. Each channel includes a four-terminal shunt, 55.7 V/6.0 V OV/UVLO ladder, hardware current thresholds, timer, bootstrap, replaceable PU/PD resistors, DNP slew/snubber sites, independent remote-temperature diode, local common-cathode inductive clamp, IMON scaling/filtering, default-off CTL p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"
- note removed: "Outputs capture notes: - Source traces: PB-100-high-medium-output-baseline-trace.csv, PB-100-high-medium-output-freeze-review.csv, PB-100-low-current-output-baseline-trace.csv, PB-100-low-current-output-freeze-review.csv, PB-100-output-stage-value-freeze-checklist.csv, PB-100-output-stage-value-derivation-precheck.csv, PB-100-output-stage-closeout-precheck.csv - OUT1 through OUT10 remain generic 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"
- title: PB-100 Outputs 1-10 -> PB-100 Generic High-Side Outputs 1–10 — Rev.1 EVT
